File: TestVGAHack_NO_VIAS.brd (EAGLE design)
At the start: 18.3 x 7.9 mm, 0 parts

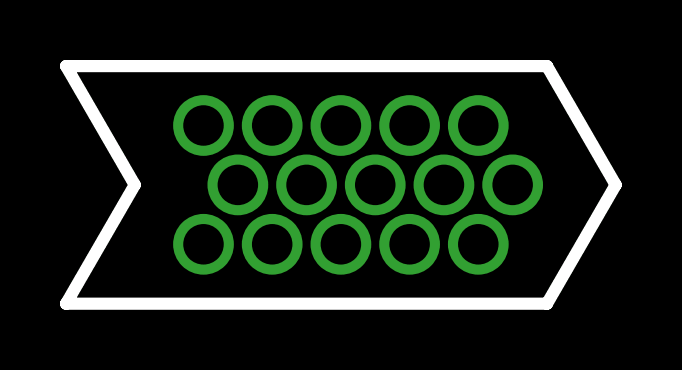
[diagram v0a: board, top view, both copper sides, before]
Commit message: Two VGA's at the same time
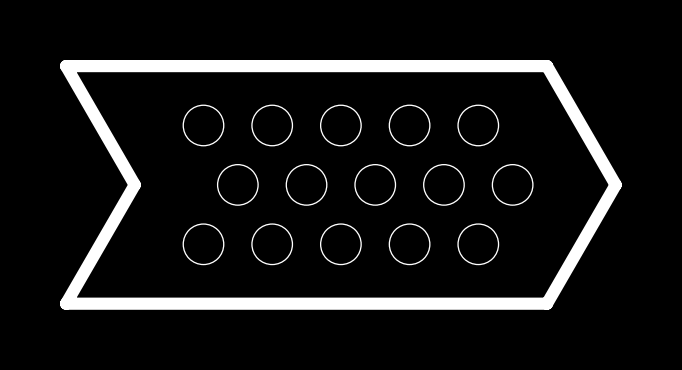
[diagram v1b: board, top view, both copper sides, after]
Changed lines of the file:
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@@
 <setting verticaltext="up"/>
 </settings>
-<grid distance="1.98" unitdist="mm" unit="mm" style="lines" multiple="1" display="yes" altdistance="1.98" altunitdist="mm" altunit="mm"/>
+<grid distance="1.145" unitdist="mm" unit="mm" style="lines" multiple="2" display="yes" altdistance="1.98" altunitdist="mm" altunit="mm"/>
 <layers>
 <layer number="1" name="Top" color="4" fill="1" visible="yes" active="yes"/>
@@
 <wire x1="-4.58" y1="1.98" x2="11.45" y2="1.98" width="0.4064" layer="20"/>
 <wire x1="-4.58" y1="-5.94" x2="11.45" y2="-5.94" width="0.4064" layer="20"/>
+<hole x="0" y="0" drill="1.35"/>
+<hole x="2.29" y="0" drill="1.35"/>
+<hole x="4.58" y="0" drill="1.35"/>
+<hole x="6.87" y="0" drill="1.35"/>
+<hole x="9.16" y="0" drill="1.35"/>
+<hole x="0" y="-3.96" drill="1.35"/>
+<hole x="1.145" y="-1.98" drill="1.35"/>
+<hole x="3.435" y="-1.98" drill="1.35"/>
+<hole x="5.725" y="-1.98" drill="1.35"/>
+<hole x="8.015" y="-1.98" drill="1.35"/>
+<hole x="10.305" y="-1.98" drill="1.35"/>
+<hole x="2.29" y="-3.96" drill="1.35"/>
+<hole x="4.58" y="-3.96" drill="1.35"/>
+<hole x="6.87" y="-3.96" drill="1.35"/>
+<hole x="9.16" y="-3.96" drill="1.35"/>
 </plain>
 <attributes>
@@
 </elements>
 <signals>
-<signal name="S$1">
-<via x="0" y="0" extent="1-16" drill="1.35"/>
-</signal>
-<signal name="S$2">
-<via x="1.145" y="-1.98" extent="1-16" drill="1.35"/>
-</signal>
-<signal name="S$3">
-<via x="0" y="-3.96" extent="1-16" drill="1.35"/>
-</signal>
-<signal name="S$4">
-<via x="2.29" y="0" extent="1-16" drill="1.35"/>
-</signal>
-<signal name="S$5">
-<via x="4.58" y="0" extent="1-16" drill="1.35"/>
-</signal>
-<signal name="S$6">
-<via x="6.87" y="0" extent="1-16" drill="1.35"/>
-</signal>
-<signal name="S$7">
-<via x="9.16" y="0" extent="1-16" drill="1.35"/>
-</signal>
-<signal name="S$8">
-<via x="2.29" y="-3.96" extent="1-16" drill="1.35"/>
-</signal>
-<signal name="S$9">
-<via x="4.58" y="-3.96" extent="1-16" drill="1.35"/>
-</signal>
-<signal name="S$10">
-<via x="6.87" y="-3.96" extent="1-16" drill="1.35"/>
-</signal>
-<signal name="S$11">
-<via x="9.16" y="-3.96" extent="1-16" drill="1.35"/>
-</signal>
-<signal name="S$12">
-<via x="3.435" y="-1.98" extent="1-16" drill="1.35"/>
-</signal>
-<signal name="S$13">
-<via x="5.725" y="-1.98" extent="1-16" drill="1.35"/>
-</signal>
-<signal name="S$14">
-<via x="8.015" y="-1.98" extent="1-16" drill="1.35"/>
-</signal>
-<signal name="S$15">
-<via x="10.305" y="-1.98" extent="1-16" drill="1.35"/>
-</signal>
 </signals>
 </board>
